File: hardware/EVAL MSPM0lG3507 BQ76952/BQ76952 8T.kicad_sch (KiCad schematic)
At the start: 56 parts, among them U11 FCX495, U13 PBQ76952PFBT, U14 FCX495

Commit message: adding link for BBQ (SPI)
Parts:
- U13: Digikey (none) -> https://www.digikey.com/en/products/detail/texas-instrument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; mouser https://www.mouser.com/ProductDetail/Texas-Instruments/BQ7695202PFBR?qs=iLbezkQI%252BsjAH4%2FOlFMlZA%3D%3D -> https://www.mouser.com/ProductDetail/Texas-Instruments/BQ7697204PFBR?qs=mELouGlnn3d1bfb90Grt5w%3D%3D
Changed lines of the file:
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@@
 			)
 		)
-		(property "mouser" "https://www.mouser.com/ProductDetail/Texas-Instruments/BQ7695202PFBR?qs=iLbezkQI%252BsjAH4%2FOlFMlZA%3D%3D"
+		(property "mouser" "https://www.mouser.com/ProductDetail/Texas-Instruments/BQ7697204PFBR?qs=mELouGlnn3d1bfb90Grt5w%3D%3D"
 			(at 142.24 73.66 0)
 			(effects
@@
 			(at 142.24 73.66 0)
 			(effects
+				(font
+					(size 1.27 1.27)
+				)
+				(hide yes)
+			)
+		)
+		(property "Digikey" "https://www.digikey.com/en/products/detail/texas-instruments/BQ7697204PFBR/22077490?s=N4IgTCBcDaIEIEUDsA2AnEsAGALCAugL5A"
+			(at 142.24 73.66 0)
+			(effects

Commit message: sorry
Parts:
- U13: Digikey https://www.digikey.com/en/products/detail/texas-instrument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 -> (none); mouser https://www.mouser.com/ProductDetail/Texas-Instruments/BQ7697204PFBR?qs=mELouGlnn3d1bfb90Grt5w%3D%3D -> https://www.mouser.com/ProductDetail/Texas-Instruments/BQ7695204PFBR?qs=iLbezkQI%252BsiEQall6bGLHw%3D%3D&srsltid=AfmBOortQS0ZF7nyGONpPu2GM9H0Yt_aAZOvNG6JzQEqbOzrseuaG7sd
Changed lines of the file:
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@@
 			)
 		)
-		(property "mouser" "https://www.mouser.com/ProductDetail/Texas-Instruments/BQ7697204PFBR?qs=mELouGlnn3d1bfb90Grt5w%3D%3D"
+		(property "mouser" "https://www.mouser.com/ProductDetail/Texas-Instruments/BQ7695204PFBR?qs=iLbezkQI%252BsiEQall6bGLHw%3D%3D&srsltid=AfmBOortQS0ZF7nyGONpPu2GM9H0Yt_aAZOvNG6JzQEqbOzrseuaG7sd"
 			(at 142.24 73.66 0)
 			(effects
@@
 			(at 142.24 73.66 0)
 			(effects
-				(font
-					(size 1.27 1.27)
-				)
-				(hide yes)
-			)
-		)
-		(property "Digikey" "https://www.digikey.com/en/products/detail/texas-instruments/BQ7697204PFBR/22077490?s=N4IgTCBcDaIEIEUDsA2AnEsAGALCAugL5A"
-			(at 142.24 73.66 0)
-			(effects

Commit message: reordered can sub section
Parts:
- removed C16: 220n, Capacitor_SMD:C_1206_3216Metric_Pad1.33x1.80mm_HandSolder, symbol Device:C_Small
- removed C58, C59: 100n, Capacitor_SMD:C_1206_3216Metric_Pad1.33x1.80mm_HandSolder, symbol Device:C_Small
- removed D2: 36V, Diode_SMD:D_SOD-123, symbol Device:D_Zener_Small
- removed R27, R46: 100k, Resistor_SMD:R_1206_3216Metric_Pad1.30x1.75mm_HandSolder, symbol Device:R_US
- removed TP1, TP18, TP7: TestPoint, TestPoint:TestPoint_Loop_D2.50mm_Drill1.0mm_LowProfile, symbol Connector:TestPoint
- removed U11: FCX495, Package_TO_SOT_SMD:SOT-89-3, symbol zzLocalLibrary:FCX485_NPN_BJT
- added C2: 10u, Capacitor_SMD:C_0805_2012Metric_Pad1.18x1.45mm_HandSolder, symbol Device:C_Small
- C1: value 100n -> 10u; footprint Capacitor_SMD:C_1206_3216Metric_Pad1.33x1.80mm_HandSolder -> Capacitor_SMD:C_0805_2012Metric_Pad1.18x1.45mm_HandSolder; mouser https://www.mouser.com/ProductDetail/Walsin/1206B104K251CT?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 -> https://www.mouser.com/ProductDetail/YAGEO/CC0805KKX7RYBB10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; specs 100nF, 250VDC, X7R, 10%, -55C, +125C -> 100nF, 250VDC, 10%, -55C, +125C; unit x1 (none) -> 0.12; unit x10 0.062 -> 0.073
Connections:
- net BAT: now also C1.1, U13.46 (CP1), U13.47 (BAT), C2.1
- net Series Sense N: now also C2.2
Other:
- note removed: "power supply input pin (50V abs max, limited by caps)"

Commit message: aec
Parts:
- added C8: 220n, Capacitor_SMD:C_1206_3216Metric_Pad1.33x1.80mm_HandSolder, symbol Device:C_Small
- added D6, D7: BAT54S, Package_TO_SOT_SMD:SOT-23-3, symbol Diode:BAT54S
- added R5: 150, Resistor_SMD:R_1206_3216Metric_Pad1.30x1.75mm_HandSolder, symbol Device:R_US
- added U1: MCP6L01Rx-xOT, Package_TO_SOT_SMD:SOT-23-5_HandSoldering, symbol Amplifier_Operational:MCP6L01Rx-xOT
- D3: unit x1 (none) -> 0.10
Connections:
- net 1N: now also C1.2, C2.2, C47.2, C55.2, C57.2, R44.2, U13.17 (VSS), C8.1, D6.1 (A), D7.1 (A), U1.5 (V-); no longer R44.1
- net 1P: now also R5.2
- net Series Sense N: no longer C1.2, C2.2, C47.2, C55.2, C57.2, U13.17 (VSS)
- net at C47.1, U13.16 (VC0): now also R44.1; no longer R44.2
- net at C30.1, C34.1, R25.2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: now also D6.3 (COM)
- net at C30.2, C34.2, R26.2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: now also D7.3 (COM)
- net at C57.1, U13.24 (REG18): now also U1.3 (+)
- new net: C8.2, D6.2 (K), D7.2 (K), U1.1, U1.4 (-)
- new net: R5.1, U1.2 (V+)
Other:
- note added: "SHOULD BE SAME POTENTIAL (think 4 wire measurement)"
- moved on the sheet: C30, C34, C57, R25, R26, R44

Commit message: clean up
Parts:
- C1, C2: footprint Capacitor_SMD:C_0805_2012Metric_Pad1.18x1.45mm_HandSolder -> Capacitor_SMD:C_1206_3216Metric_Pad1.33x1.80mm_HandSolder; mouser https://www.mouser.com/ProductDetail/YAGEO/CC0805KKX7RYBB10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 -> https://www.mouser.com/ProductDetail/Samsung-Electro-Mechan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; specs 100nF, 250VDC, 10%, -55C, +125C -> 10uF, 50VDC, X5R, 10%, -55C, +85C; unit x1 0.12 -> (none); unit x10 0.073 -> 0.07
- C30: unit x10 0.062 -> 0.042
- C36, C37, C38, C42, C43, C44, C45, C46, C47, C48, C49, C50, C51, C52, C53, C54, C55, C8: unit x10 0.05 -> 0.054

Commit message: asdasd
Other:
- note added: "TODO: external ballancing fets. target ~250mA"
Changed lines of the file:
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@@
+		)
+	)
+	(text "TODO: external ballancing fets. target ~250mA"
+		(exclude_from_sim no)
+		(at 229.87 174.752 0)
+		(effects
+			(font
+				(size 1.27 1.27)
+			)
 		)
 	)

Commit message: lbjnlj
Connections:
- net 16P: no longer R15.1, R9.2, U14.2
- net BAT: now also R15.1, R9.2, U14.2
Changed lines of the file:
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@@
+	)
+	(junction
+		(at 207.01 34.29)
+		(diameter 0)
+		(color 0 0 0 0)
 	)
 	(junction
@@
 	)
 	(junction
-		(at 187.96 34.29)
-		(diameter 0)
-		(color 0 0 0 0)
-	)
-	(junction
 		(at 90.17 146.05)
 		(diameter 0)
@@
 	)
 	(junction
+		(at 207.01 76.2)
+		(diameter 0)
+		(color 0 0 0 0)
+	)
+	(junction
 		(at 118.11 166.37)
 		(diameter 0)
@@
 	(wire
 		(pts
-			(xy 187.96 34.29) (xy 187.96 76.2)
-		)
-		(stroke
-			(width 0)
-			(type default)
-		)
-	)
-	(wire
-		(pts
-			(xy 176.53 34.29) (xy 187.96 34.29)
+			(xy 207.01 34.29) (xy 207.01 76.2)
+		)
+		(stroke
+			(width 0)
+			(type default)
+		)
+	)
+	(wire
+		(pts
+			(xy 176.53 34.29) (xy 207.01 34.29)
 		)
 		(stroke
@@
 	(wire
 		(pts
-			(xy 207.01 88.9) (xy 209.55 88.9)
-		)
-		(stroke
-			(width 0)
-			(type default)
-		)
-	)
-	(wire
-		(pts
 			(xy 96.52 82.55) (xy 102.87 82.55)
 		)
@@
 	(wire
 		(pts
+			(xy 187.96 76.2) (xy 207.01 76.2)
+		)
+		(stroke
+			(width 0)
+			(type default)
+		)
+	)
+	(wire
+		(pts
 			(xy 52.07 38.1) (xy 52.07 34.29)
 		)
@@
 	(wire
 		(pts
-			(xy 187.96 34.29) (xy 189.23 34.29)
-		)
-		(stroke
-			(width 0)
-			(type default)
-		)
-	)
-	(wire
-		(pts
 			(xy 154.94 163.83) (xy 154.94 173.99)
 		)
@@
 	(wire
 		(pts
+			(xy 207.01 34.29) (xy 212.09 34.29)
+		)
+		(stroke
+			(width 0)
+			(type default)
+		)
+	)
+	(wire
+		(pts
 			(xy 101.6 95.25) (xy 101.6 93.98)
 		)
@@
 		(pts
 			(xy 160.02 171.45) (xy 160.02 173.99)
+		)
+		(stroke
+			(width 0)
+			(type default)
+		)
+	)
+	(wire
+		(pts
+			(xy 207.01 76.2) (xy 207.01 88.9)
 		)
 		(stroke
@@
 			)
 			(justify right bottom)
-		)
-	)
-	(label "PACK+"
-		(at 209.55 88.9 0)
-		(effects
-			(font
-				(size 1.27 1.27)
-			)
-			(justify left bottom)
 		)
 	)
@@
 	(hierarchical_label "BAT"
 		(shape output)
-		(at 189.23 34.29 0)
-		(effects
-			(font
+		(at 212.09 34.29 0)
+		(effects
+			(font

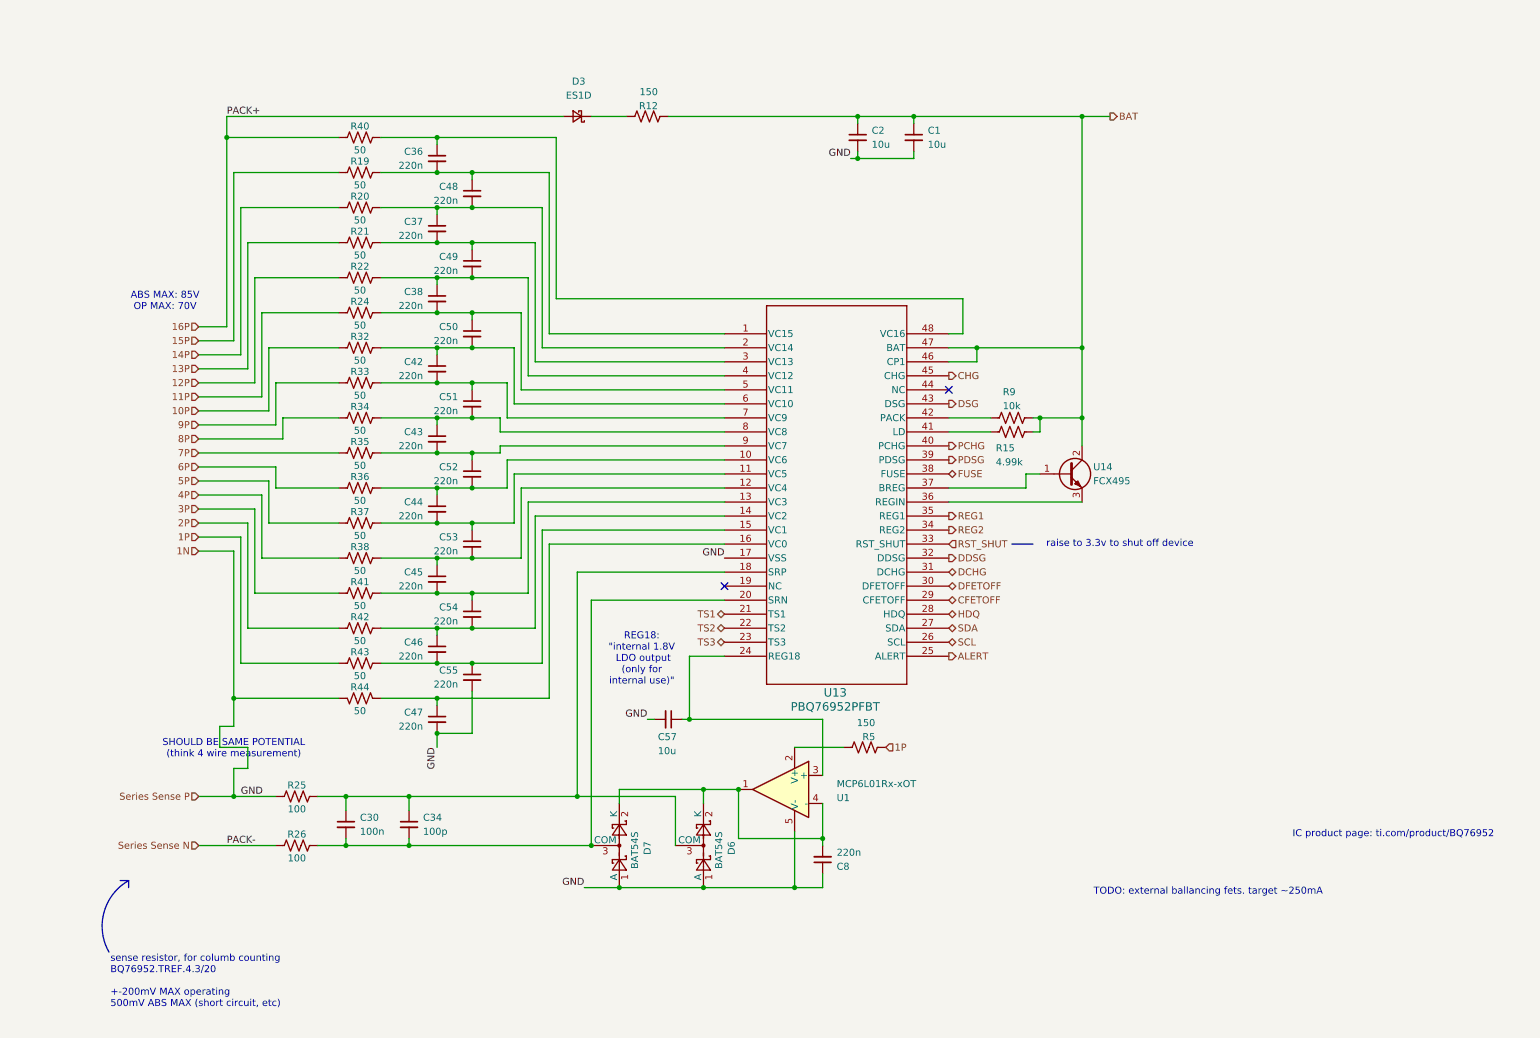
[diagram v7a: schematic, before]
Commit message: corrected immediate bugs of v3.0
need to do a endurance test of v3.0 to see if hte spi lines fail
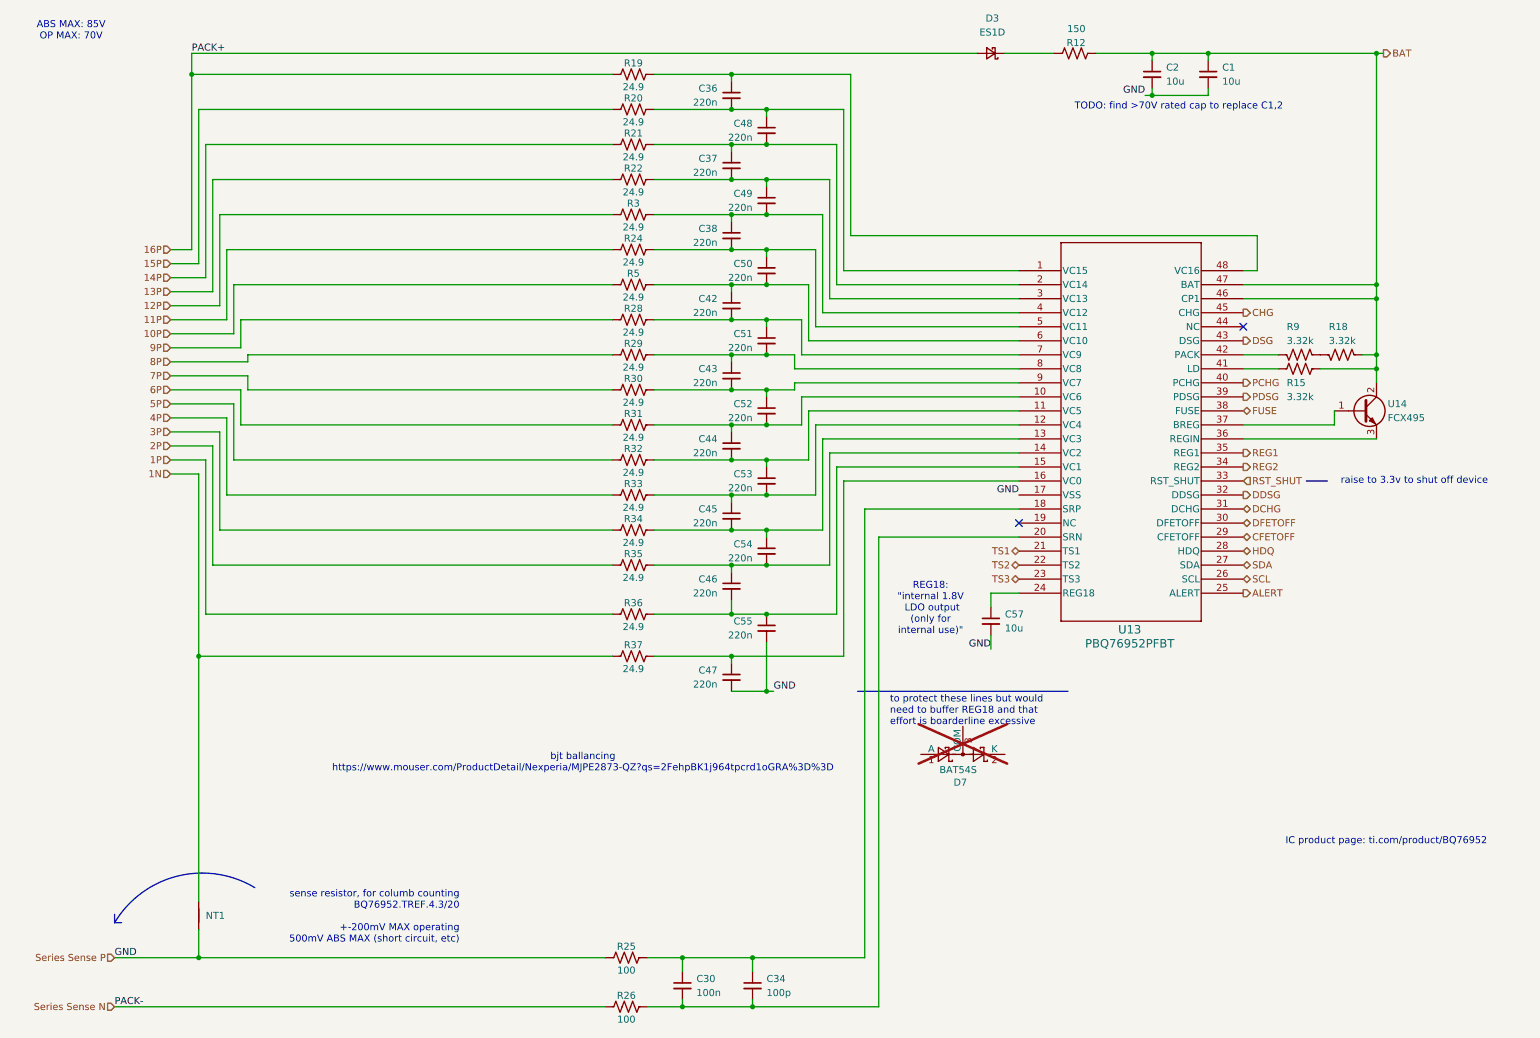
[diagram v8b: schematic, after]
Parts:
- removed C8: 220n, Capacitor_SMD:C_1206_3216Metric_Pad1.33x1.80mm_HandSolder, symbol Device:C_Small
- removed D6: BAT54S, Package_TO_SOT_SMD:SOT-23-3, symbol Diode:BAT54S
- removed R38, R40, R41, R42, R43, R44: 50, Resistor_SMD:R_1206_3216Metric_Pad1.30x1.75mm_HandSolder, symbol Device:R_US
- removed U1: MCP6L01Rx-xOT, Package_TO_SOT_SMD:SOT-23-5_HandSoldering, symbol Amplifier_Operational:MCP6L01Rx-xOT
- added NT1: NetTie_2, symbol Device:NetTie_2
- added R18: 3.32k, Resistor_SMD:R_0805_2012Metric_Pad1.20x1.40mm_HandSolder, symbol Device:R_US
- added R28, R29, R3, R30, R31: 24.9, Resistor_SMD:R_0805_2012Metric_Pad1.20x1.40mm_HandSolder, symbol Device:R_US
- D7: now not fitted; now left out of the parts list
- R15: value 4.99k -> 3.32k; footprint Resistor_SMD:R_1206_3216Metric_Pad1.30x1.75mm_HandSolder -> Resistor_SMD:R_0805_2012Metric_Pad1.20x1.40mm_HandSolder; mouser https://www.mouser.com/ProductDetail/SEI-Stackpole/RNCP1206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 -> https://www.mouser.com/ProductDetail/Walsin/WR08X3321FTL?qs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; specs 4.99kOhm, 200V, 500mW, 1%, 100PPM, -55C, +155C -> 3.32kOhm, 1%, 150V, 125mW, 100ppm, -55C, 155C; unit x1 (none) -> 0.1; unit x10 0.017 -> 0.019
- R19, R20, R21, R22, R24, R32, R33, R34, R35, R36, R37: value 50 -> 24.9; footprint Resistor_SMD:R_1206_3216Metric_Pad1.30x1.75mm_HandSolder -> Resistor_SMD:R_0805_2012Metric_Pad1.20x1.40mm_HandSolder; mouser https://www.mouser.com/ProductDetail/Panasonic/ERJ-P08F51R0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 -> https://www.mouser.com/ProductDetail/ROHM-Semiconductor/ESR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; specs 51Ohms, 660mW, 1%, 500V, 100PPM, -55C, +155C -> 24.9Ohm, 1%, anti-surge, 500mW, 150V, 100ppm, -55c, 155c
- R5: value 150 -> 24.9; footprint Resistor_SMD:R_1206_3216Metric_Pad1.30x1.75mm_HandSolder -> Resistor_SMD:R_0805_2012Metric_Pad1.20x1.40mm_HandSolder; mouser https://www.mouser.com/ProductDetail/YAGEO/AC1206FR-7W150RL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 -> https://www.mouser.com/ProductDetail/ROHM-Semiconductor/ESR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; specs 150Ohm, 500mW, 1%, 200V, -55C, +155C -> 24.9Ohm, 1%, anti-surge, 500mW, 150V, 100ppm, -55c, 155c; unit x10 0.032 -> 0.056
- R9: value 10k -> 3.32k; mouser https://www.mouser.com/ProductDetail/KOA-Speer/RK73H2ATTED1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 -> https://www.mouser.com/ProductDetail/Walsin/WR08X3321FTL?qs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; specs 10k, 150V, 250mW, 1%, 100ppm -> 3.32kOhm, 1%, 150V, 125mW, 100ppm, -55C, 155C; unit x1 0.10 -> 0.1; unit x10 0.021 -> 0.019
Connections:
- net 10P: now also R5.1; no longer R32.1
- net 12P: now also R3.1; no longer R22.1
- net 13P: now also R22.1; no longer R21.1
- net 14P: now also R21.1; no longer R20.1
- net 15P: now also R20.1; no longer R19.1
- net 16P: now also R19.1
- net 1N: now also R37.1, NT1.1; no longer C1.2, C2.2, C47.2, C55.2, C57.2, D7.1 (A), R25.1, U13.17 (VSS)
- net 1P: now also R36.1; no longer R5.2
- net 2P: now also R35.1
- net 3P: now also R34.1
- net 4P: now also R33.1
- net 5P: now also R32.1; no longer R37.1
- net 6P: now also R31.1; no longer R36.1
- net 7P: now also R30.1; no longer R35.1
- net 8P: now also R29.1; no longer R34.1
- net 9P: now also R28.1; no longer R33.1
- net BAT: now also R15.2, R18.2; no longer R15.1, R9.2
- net at C43.2, C52.1, U13.9 (VC7): now also R30.2; no longer R35.2
- net at U13.41 (LD): now also R15.1; no longer R15.2
- net at C43.1, C51.2, U13.8 (VC8): now also R29.2; no longer R34.2
- net at C42.2, C51.1, U13.7 (VC9): now also R28.2; no longer R33.2
- net at C30.2, C34.2, R26.2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: no longer D7.3 (COM)
- net at C44.2, C53.1, U13.11 (VC5): now also R32.2; no longer R37.2
- net at C42.1, C50.2, U13.6 (VC10): now also R5.2; no longer R32.2
- net at C36.2, C48.1, U13.1 (VC15): now also R20.2; no longer R19.2
- net at C45.1, C53.2, U13.12 (VC4): now also R33.2
- net at C45.2, C54.1, U13.13 (VC3): now also R34.2
- net at C38.1, C49.2, U13.4 (VC12): now also R3.2; no longer R22.2
- net at C37.1, C48.2, U13.2 (VC14): now also R21.2; no longer R20.2
- net at C37.2, C49.1, U13.3 (VC13): now also R22.2; no longer R21.2
- net at C44.1, C52.2, U13.10 (VC6): now also R31.2; no longer R36.2
- net at C46.1, C54.2, U13.14 (VC2): now also R35.2
- net at C46.2, C55.1, U13.15 (VC1): now also R36.2
- net at C47.1, U13.16 (VC0): now also R37.2
- net at C36.1, U13.48 (VC16): now also R19.2
- new net: R18.1, R9.2
- new net Series Sense P: C1.2, C2.2, C47.2, C55.2, C57.2, NT1.2, R25.1, U13.17 (VSS)
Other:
- note added: "TODO: find >70V rated cap to replace C1,2"
- note added: "bjt ballancing https://www.mouser.com/ProductDetail/Nexperia/MJPE2873-QZ?qs=2FehpBK1j964tpcrd1oGRA%3D%3D"
- note added: "to protect these lines but would need to buffer REG18 and that effort is boarderline excessive"
- note removed: "SHOULD BE SAME POTENTIAL (think 4 wire measurement)"
- note removed: "TODO: external ballancing fets. target ~250mA"
- moved on the sheet: C1, C2, C30, C34, C36, C37, C38, C42, C43, C44, C45, C46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
